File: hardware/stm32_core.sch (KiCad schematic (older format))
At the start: 33 parts

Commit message: update for cherry key,
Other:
- moved on the sheet: C?, D?, JP?, R?, SW?, U?, Y?

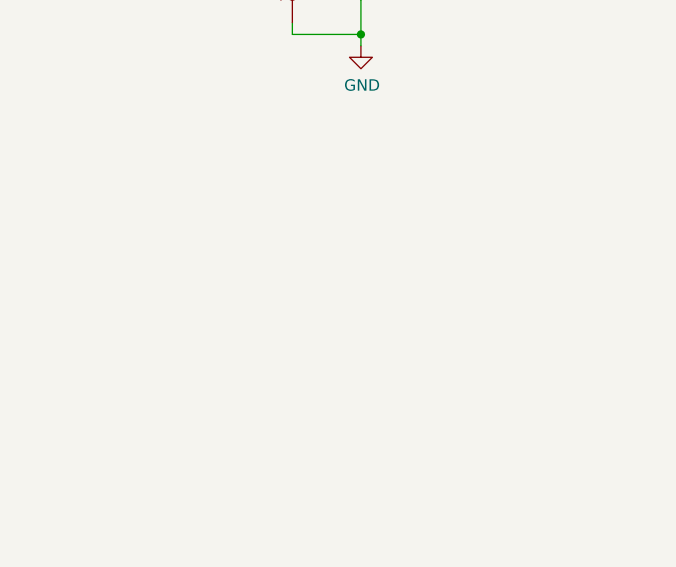
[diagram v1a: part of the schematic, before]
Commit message: update for cherry key,wd
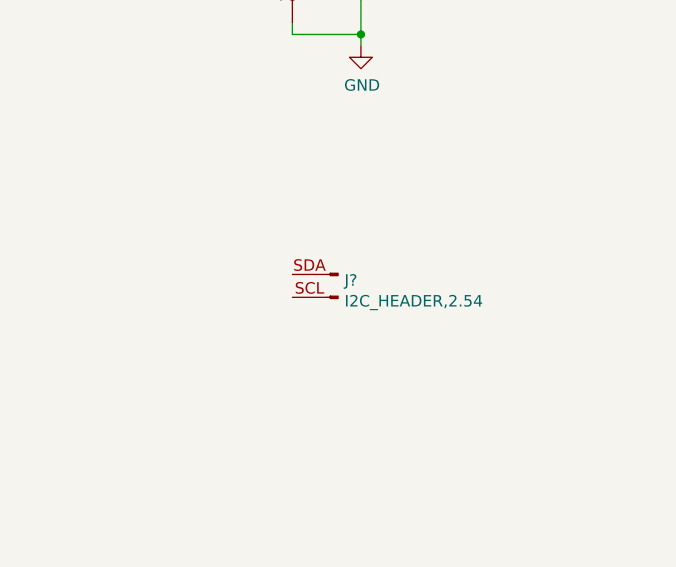
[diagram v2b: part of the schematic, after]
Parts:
- added J?: I2C_HEADER,2.54, Connector_PinHeader_2.54mm:PinHeader_1x02_P2.54mm_Vertical, symbol taobao-components:I2C_HEADER,2.54
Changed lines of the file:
@@
 NoConn ~ 1900 7100
 NoConn ~ 1900 7300
+$Comp
+L taobao-components:I2C_HEADER,2.54 J?
+U 1 1 5D064141
+P 7850 5600
+F 0 "J?" H 7822 5624 50  0000 R CNN
+F 1 "I2C_HEADER,2.54" H 7822 5533 50  0000 R CNN
+F 2 "Connector_PinHeader_2.54mm:PinHeader_1x02_P2.54mm_Vertical" H 7850 5200 50  0001 C CNN
+F 3 "" H 7850 5550 50  0001 C CNN
+	1    7850 5600
+	-1   0    0    -1
+$EndComp
 $EndSCHEMATC

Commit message: update for power symbol,
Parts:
- added R? (x2): R472,0603, Resistor_SMD:R_0603_1608Metric_Pad1.05x0.95mm_HandSolder, symbol taobao-r:R472,0603
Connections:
- net +3V3: no longer C?.1, C?.1, C?.1, C?.1, JP?.3 (B), JP?.3 (B), R?.1, U?.1 (VBAT), U?.24 (VDD_1), U?.36 (VDD_2), U?.48 (VDD_3), U?.9 (VDDA)
- net PB6: now also J?.SCL, R?.1
- net PB7: now also J?.SDA, R?.1
- new net Vstm32: C?.1, C?.1, C?.1, C?.1, JP?.3 (B), JP?.3 (B), R?.1, R?.2, R?.2, U?.1 (VBAT), U?.24 (VDD_1), U?.36 (VDD_2), U?.48 (VDD_3), U?.9 (VDDA)
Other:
- moved on the sheet: J?
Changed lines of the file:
@@
 Wire Wire Line
 	3500 1300 3500 1850
-Wire Wire Line
-	3300 5150 3300 5250
 $Comp
 L power:GND #PWR?
@@
 Wire Wire Line
 	3300 5450 3300 5550
-Wire Wire Line
-	3750 5150 3750 5250
 $Comp
 L power:GND #PWR?
@@
 Wire Wire Line
 	4150 5450 4150 5550
-Wire Wire Line
-	4600 5150 4600 5250
 $Comp
 L power:GND #PWR?
@@
 Wire Wire Line
 	7950 4350 7950 4500
-Wire Wire Line
-	7550 1200 7550 1500
 $Comp
 L taobao-r:R104 R?
@@
 Wire Wire Line
 	7550 2100 7550 1900
-Wire Wire Line
-	8400 1200 8400 1500
 $Comp
 L power:GND #PWR?
@@
 Text Label 1200 2700 2    50   ~ 0
 VCC3V3
-Wire Wire Line
-	850  2500 850  2700
-$Comp
-L power:+3V3 #PWR?
-U 1 1 5BCAD5BF
-P 850 2500
-F 0 "#PWR?" H 850 2350 50  0001 C CNN
-F 1 "+3V3" H 900 2700 50  0000 C CNN
-F 2 "" H 850 2500 50  0001 C CNN
-F 3 "" H 850 2500 50  0001 C CNN
-	1    850  2500
-	1    0    0    -1
-$EndComp
-$Comp
-L power:+3V3 #PWR?
-U 1 1 5BCBE3DE
-P 3300 5150
-F 0 "#PWR?" H 3300 5000 50  0001 C CNN
-F 1 "+3V3" H 3350 5350 50  0000 C CNN
-F 2 "" H 3300 5150 50  0001 C CNN
-F 3 "" H 3300 5150 50  0001 C CNN
-	1    3300 5150
-	1    0    0    -1
-$EndComp
-$Comp
-L power:+3V3 #PWR?
-U 1 1 5BCE7C1D
-P 3750 5150
-F 0 "#PWR?" H 3750 5000 50  0001 C CNN
-F 1 "+3V3" H 3800 5350 50  0000 C CNN
-F 2 "" H 3750 5150 50  0001 C CNN
-F 3 "" H 3750 5150 50  0001 C CNN
-	1    3750 5150
-	1    0    0    -1
-$EndComp
-$Comp
-L power:+3V3 #PWR?
-U 1 1 5BCE7C66
-P 4150 5150
-F 0 "#PWR?" H 4150 5000 50  0001 C CNN
-F 1 "+3V3" H 4200 5350 50  0000 C CNN
-F 2 "" H 4150 5150 50  0001 C CNN
-F 3 "" H 4150 5150 50  0001 C CNN
-	1    4150 5150
-	1    0    0    -1
-$EndComp
-$Comp
-L power:+3V3 #PWR?
-U 1 1 5BCE7CAF
-P 4600 5150
-F 0 "#PWR?" H 4600 5000 50  0001 C CNN
-F 1 "+3V3" H 4650 5350 50  0000 C CNN
-F 2 "" H 4600 5150 50  0001 C CNN
-F 3 "" H 4600 5150 50  0001 C CNN
-	1    4600 5150
-	1    0    0    -1
-$EndComp
 $Comp
 L power:+3V3 #PWR?
@@
 	0    -1   -1   0
 $EndComp
-$Comp
-L power:+3V3 #PWR?
-U 1 1 5BCF3126
-P 7950 3350
-F 0 "#PWR?" H 7950 3200 50  0001 C CNN
-F 1 "+3V3" H 8000 3550 50  0000 C CNN
-F 2 "" H 7950 3350 50  0001 C CNN
-F 3 "" H 7950 3350 50  0001 C CNN
-	1    7950 3350
-	1    0    0    -1
-$EndComp
-$Comp
-L power:+3V3 #PWR?
-U 1 1 5BCF394E
-P 8400 1200
-F 0 "#PWR?" H 8400 1050 50  0001 C CNN
-F 1 "+3V3" H 8450 1400 50  0000 C CNN
-F 2 "" H 8400 1200 50  0001 C CNN
-F 3 "" H 8400 1200 50  0001 C CNN
-	1    8400 1200
-	1    0    0    -1
-$EndComp
-$Comp
-L power:+3V3 #PWR?
-U 1 1 5BCF3997
-P 7550 1200
-F 0 "#PWR?" H 7550 1050 50  0001 C CNN
-F 1 "+3V3" H 7600 1400 50  0000 C CNN
-F 2 "" H 7550 1200 50  0001 C CNN
-F 3 "" H 7550 1200 50  0001 C CNN
-	1    7550 1200
-	1    0    0    -1
-$EndComp
 Wire Wire Line
 	1200 2700 850  2700
@@
 	1    0    0    -1
 $EndComp
-Wire Wire Line
-	4150 5150 4150 5250
 $Comp
 L taobao-c:C104,0603 C?
@@
 L taobao-components:I2C_HEADER,2.54 J?
 U 1 1 5D064141
-P 7850 5600
-F 0 "J?" H 7822 5624 50  0000 R CNN
-F 1 "I2C_HEADER,2.54" H 7822 5533 50  0000 R CNN
-F 2 "Connector_PinHeader_2.54mm:PinHeader_1x02_P2.54mm_Vertical" H 7850 5200 50  0001 C CNN
-F 3 "" H 7850 5550 50  0001 C CNN
-	1    7850 5600
+P 8700 5850
+F 0 "J?" H 8672 5874 50  0000 R CNN
+F 1 "I2C_HEADER,2.54" H 8672 5783 50  0000 R CNN
+F 2 "Connector_PinHeader_2.54mm:PinHeader_1x02_P2.54mm_Vertical" H 8700 5450 50  0001 C CNN
+F 3 "" H 8700 5800 50  0001 C CNN
+	1    8700 5850
 	-1   0    0    -1
 $EndComp
+$Comp
+L taobao-r:R472,0603 R?
+U 1 1 5D07DB4D
+P 7950 5600
+F 0 "R?" H 7891 5554 50  0000 R CNN
+F 1 "R472,0603" H 7891 5645 50  0000 R CNN
+F 2 "Resistor_SMD:R_0603_1608Metric_Pad1.05x0.95mm_HandSolder" H 7950 5600 50  0001 C CNN
+F 3 "~" H 7950 5600 50  0001 C CNN
+	1    7950 5600
+	-1   0    0    1
+$EndComp
+$Comp
+L taobao-r:R472,0603 R?
+U 1 1 5D07E05F
+P 7700 5550
+F 0 "R?" H 7641 5504 50  0000 R CNN
+F 1 "R472,0603" H 7641 5595 50  0000 R CNN
+F 2 "Resistor_SMD:R_0603_1608Metric_Pad1.05x0.95mm_HandSolder" H 7700 5550 50  0001 C CNN
+F 3 "~" H 7700 5550 50  0001 C CNN
+	1    7700 5550
+	-1   0    0    1
+$EndComp
+Wire Wire Line
+	8500 5900 7700 5900
+Wire Wire Line
+	7700 5900 7700 5650
+Text Label 7100 5800 0    50   ~ 0
+PB7
+Text Label 7100 5900 0    50   ~ 0
+PB6
+Wire Wire Line
+	7700 5900 7100 5900
+Connection ~ 7700 5900
+Wire Wire Line
+	7100 5800 7950 5800
+Wire Wire Line
+	7950 5700 7950 5800
+Connection ~ 7950 5800
+Wire Wire Line
+	7950 5800 8500 5800
+Text Label 8200 5200 2    50   ~ 0
+VCC3V3
+Wire Wire Line
+	7700 5200 7700 5400
+Wire Wire Line
+	7700 5200 8200 5200
+Wire Wire Line
+	7700 5400 7950 5400
+Wire Wire Line
+	7950 5400 7950 5500
+Connection ~ 7700 5400
+Wire Wire Line
+	7700 5400 7700 5450
+$Comp
+L my_power:Vstm32 #PWR?
+U 1 1 5D0F9DAF
+P 850 2100
+F 0 "#PWR?" H 850 1950 50  0001 C CNN
+F 1 "Vstm32" H 855 2273 50  0000 C CNN
+F 2 "" H 850 2100 50  0001 C CNN
+F 3 "" H 850 2100 50  0001 C CNN
+	1    850  2100
+	1    0    0    -1
+$EndComp
+Wire Wire Line
+	850  2100 850  2700
+$Comp
+L my_power:Vstm32 #PWR?
+U 1 1 5D11BE36
+P 3950 5050
+F 0 "#PWR?" H 3950 4900 50  0001 C CNN
+F 1 "Vstm32" H 3955 5223 50  0000 C CNN
+F 2 "" H 3950 5050 50  0001 C CNN
+F 3 "" H 3950 5050 50  0001 C CNN
+	1    3950 5050
+	1    0    0    -1
+$EndComp
+Wire Wire Line
+	3950 5050 3950 5150
+Wire Wire Line
+	3950 5150 3750 5150
+Wire Wire Line
+	3300 5150 3300 5250
+Wire Wire Line
+	3750 5250 3750 5150
+Connection ~ 3750 5150
+Wire Wire Line
+	3750 5150 3300 5150
+Wire Wire Line
+	3950 5150 4150 5150
+Wire Wire Line
+	4600 5150 4600 5250
+Connection ~ 3950 5150
+Wire Wire Line
+	4150 5250 4150 5150
+Connection ~ 4150 5150
+Wire Wire Line
+	4150 5150 4600 5150
+$Comp
+L my_power:Vstm32 #PWR?
+U 1 1 5D134211
+P 7950 3350
+F 0 "#PWR?" H 7950 3200 50  0001 C CNN
+F 1 "Vstm32" H 7955 3523 50  0000 C CNN
+F 2 "" H 7950 3350 50  0001 C CNN
+F 3 "" H 7950 3350 50  0001 C CNN
+	1    7950 3350
+	1    0    0    -1
+$EndComp
+$Comp
+L my_power:Vstm32 #PWR?
+U 1 1 5D136523
+P 7950 1000
+F 0 "#PWR?" H 7950 850 50  0001 C CNN
+F 1 "Vstm32" H 7955 1173 50  0000 C CNN
+F 2 "" H 7950 1000 50  0001 C CNN
+F 3 "" H 7950 1000 50  0001 C CNN
+	1    7950 1000
+	1    0    0    -1
+$EndComp
+Wire Wire Line
+	7950 1000 7950 1150
+Wire Wire Line
+	7950 1150 7550 1150
+Wire Wire Line
+	7550 1150 7550 1500
+Wire Wire Line
+	7950 1150 8400 1150
+Wire Wire Line
+	8400 1150 8400 1500
+Connection ~ 7950 1150
 $EndSCHEMATC

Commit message: update,
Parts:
- gave numbers to parts that had none: 36

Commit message: update,
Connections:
- net PA1 renamed ROW1
- net PA10 renamed TTL_RX
- net PA11 renamed USB_N
- net PA12 renamed USB_P
- net PA2 renamed ROW2
- net PA3 renamed ROW3
- net PA4 renamed ROW4
- net PA5 renamed COL1
- net PA6 renamed WS2812_OUT
- net PA7 renamed COL2
- net PA8 renamed COL3
- net PA9 renamed TTL_TX
- net PB0 renamed USR_BTN1
- net PB1 renamed USR_BTN2
- net PB10 renamed ROT_ENC_SW1
- net PB11 renamed ROT_ENC_A2
- net PB12 renamed ROT_ENC_B2
- net PB13 renamed ROT_ENC_SW2
- net PB14 renamed USR_STA2
- net PB15 renamed USR_STA3
- net PB3 renamed USR_BTN3
- net PB4 renamed USR_BTN4
- net PB5 renamed USR_STA1
- net PB8 renamed ROT_ENC_A1
- net PB9 renamed ROT_ENC_B1
- net PC14 renamed BUZZER
- net SWIO renamed SWDIO
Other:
- moved on the sheet: C10, C11, C12, C13, C14, C15, C16, C17, C18, C2, C7, C8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

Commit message: update,
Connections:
- net PA0 is gone; now on net BUZZER: U1.10 (PA0)
- net PB6 is gone; now on net SCL: J1.SCL, R4.1, U1.42 (PB6)
- net PB7 is gone; now on net SDA: J1.SDA, R5.1, U1.43 (PB7)
- net BUZZER: no longer C18.1, U1.3 (PC14), Y2.2
- new net PC14: C18.1, U1.3 (PC14), Y2.2
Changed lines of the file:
@@
-	1    0    0    -1
-$EndComp
-Wire Wire Line
-	8250 5200 8250 5650
-Text Label 7850 5200 3    50   ~ 0
-PC15
-Wire Wire Line
-	7850 5200 7850 5650
-Text Label 8250 5200 3    50   ~ 0
-PC14
-Wire Wire Line
-	8250 6050 8250 5950
-Wire Wire Line
-	7850 6050 7850 5950
-Wire Wire Line
-	8050 6050 8250 6050
-Wire Wire Line
-	8050 6050 7850 6050
-Connection ~ 8050 6050
-Wire Wire Line
-	8050 6200 8050 6050
-Wire Wire Line
-	8150 6200 8050 6200
-$Comp
-L power:GND #PWR017
-U 1 1 5BCC0C02
-P 8150 6200
-F 0 "#PWR017" H 8150 5950 50  0001 C CNN
-F 1 "GND" H 8155 6027 50  0000 C CNN
-F 2 "" H 8150 6200 50  0001 C CNN
-F 3 "" H 8150 6200 50  0001 C CNN
-	1    8150 6200
-	0    -1   -1   0
-$EndComp
-Wire Wire Line
-	7850 5650 7950 5650
-Connection ~ 7850 5650
-Wire Wire Line
-	7850 5750 7850 5650
-Wire Wire Line
-	8250 5650 8150 5650
-Connection ~ 8250 5650
-Wire Wire Line
-	8250 5750 8250 5650
-$Comp
-L taobao-c:C20pf C18
-U 1 1 5BCBF22D
-P 8250 5850
-F 0 "C18" V 8021 5850 50  0000 C CNN
-F 1 "C20pf" V 8112 5850 50  0000 C CNN
-F 2 "Capacitor_SMD:C_0603_1608Metric_Pad1.05x0.95mm_HandSolder" H 8250 5850 50  0001 C CNN
-F 3 "~" H 8250 5850 50  0001 C CNN
-	1    8250 5850
-	1    0    0    -1
-$EndComp
-$Comp
-L taobao-c:C20pf C17
-U 1 1 5BCBF1ED
-P 7850 5850
-F 0 "C17" V 7621 5850 50  0000 C CNN
-F 1 "C20pf" V 7712 5850 50  0000 C CNN
-F 2 "Capacitor_SMD:C_0603_1608Metric_Pad1.05x0.95mm_HandSolder" H 7850 5850 50  0001 C CNN
-F 3 "~" H 7850 5850 50  0001 C CNN
-	1    7850 5850
-	1    0    0    -1
-$EndComp
-$Comp
-L taobao-components:O_EPSON_32.768K Y2
-U 1 1 5BCBF11C
-P 8050 5650
-F 0 "Y2" V 8004 5738 50  0000 L CNN
-F 1 "O32.768K" V 8095 5738 50  0000 L CNN
-F 2 "footprint-lib:MC-306" H 8050 5650 50  0001 C CNN
-F 3 "~" H 8050 5650 50  0001 C CNN
-	1    8050 5650
 	1    0    0    -1
 $EndComp
@@
 Wire Wire Line
 	9650 5950 10200 5950
-Text Label 9900 5350 2    50   ~ 0
-VCC3V3
 Wire Wire Line
 	9400 5350 9400 5550
-Wire Wire Line
-	9400 5350 9900 5350
 Wire Wire Line
 	9400 5550 9650 5550
@@
 Connection ~ 9700 1050
 Text Label 1650 650  2    50   ~ 0
-SDA
+PB7
 Text Label 1650 750  2    50   ~ 0
-SCL
+PB6
 Text HLabel 1100 650  0    50   Input ~ 0
 SDA
@@
 PB15
 Text Label 1650 4250 2    50   ~ 0
-PC14
+PA0
 Text HLabel 1100 4550 0    50   Input ~ 0
 SWCLK
@@
 Text Label 1650 5000 2    50   ~ 0
 PA11
+$Comp
+L my_power:Vstm32 #PWR?
+U 1 1 5D45FAEE
+P 9400 5350
+F 0 "#PWR?" H 9400 5200 50  0001 C CNN
+F 1 "Vstm32" H 9405 5523 50  0000 C CNN
+F 2 "" H 9400 5350 50  0001 C CNN
+F 3 "" H 9400 5350 50  0001 C CNN
+	1    9400 5350
+	1    0    0    -1
+$EndComp
+$Comp
+L taobao-components:O_EPSON_32.768K Y2
+U 1 1 5BCBF11C
+P 8050 5650
+F 0 "Y2" V 8004 5738 50  0000 L CNN
+F 1 "O32.768K" V 8095 5738 50  0000 L CNN
+F 2 "footprint-lib:MC-306" H 8050 5650 50  0001 C CNN
+F 3 "~" H 8050 5650 50  0001 C CNN
+	1    8050 5650
+	1    0    0    -1
+$EndComp
+$Comp
+L taobao-c:C20pf C17
+U 1 1 5BCBF1ED
+P 7850 5850
+F 0 "C17" V 7621 5850 50  0000 C CNN
+F 1 "C20pf" V 7712 5850 50  0000 C CNN
+F 2 "Capacitor_SMD:C_0603_1608Metric_Pad1.05x0.95mm_HandSolder" H 7850 5850 50  0001 C CNN
+F 3 "~" H 7850 5850 50  0001 C CNN
+	1    7850 5850
+	1    0    0    -1
+$EndComp
+$Comp
+L taobao-c:C20pf C18
+U 1 1 5BCBF22D
+P 8250 5850
+F 0 "C18" V 8021 5850 50  0000 C CNN
+F 1 "C20pf" V 8112 5850 50  0000 C CNN
+F 2 "Capacitor_SMD:C_0603_1608Metric_Pad1.05x0.95mm_HandSolder" H 8250 5850 50  0001 C CNN
+F 3 "~" H 8250 5850 50  0001 C CNN
+	1    8250 5850
+	1    0    0    -1
+$EndComp
+Wire Wire Line
+	8250 5750 8250 5650
+Wire Wire Line
+	8250 5650 8150 5650
+Wire Wire Line
+	7850 5750 7850 5650
+Wire Wire Line
+	7850 5650 7950 5650
+$Comp
+L power:GND #PWR017
+U 1 1 5BCC0C02
+P 8150 6200
+F 0 "#PWR017" H 8150 5950 50  0001 C CNN
+F 1 "GND" H 8155 6027 50  0000 C CNN
+F 2 "" H 8150 6200 50  0001 C CNN
+F 3 "" H 8150 6200 50  0001 C CNN
+	1    8150 6200
+	0    -1   -1   0
+$EndComp
+Wire Wire Line
+	8150 6200 8050 6200
+Wire Wire Line
+	8050 6200 8050 6050
+Wire Wire Line
+	8050 6050 7850 6050
+Connection ~ 8050 6050
+Wire Wire Line
+	8050 6050 8250 6050
+Wire Wire Line
+	7850 6050 7850 5950
+Wire Wire Line
+	8250 6050 8250 5950
+Text Label 8250 5200 3    50   ~ 0
+PC14
+Connection ~ 7850 5650
+Wire Wire Line
+	7850 5200 7850 5650
+Text Label 7850 5200 3    50   ~ 0
+PC15
+Connection ~ 8250 5650
+Wire Wire Line
+	8250 5200 8250 5650
 $EndSCHEMATC

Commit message: update,
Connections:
- net OSCIN renamed OSC_N
- net OSC_N: now also U1.6 (OSCOUT); no longer U1.5 (OSCIN)
- net OSCOUT renamed OSC_P
- net OSC_P: now also U1.5 (OSCIN); no longer U1.6 (OSCOUT)
- net PC14 renamed OSC32K_N
- net OSC32K_N: now also U1.4 (PC15); no longer U1.3 (PC14)
- net PC15 renamed OSC32K_P
- net OSC32K_P: now also U1.3 (PC14); no longer U1.4 (PC15)
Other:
- moved on the sheet: C3, C4, C5, C6
